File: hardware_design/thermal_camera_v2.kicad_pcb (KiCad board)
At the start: 2 copper layers, 69 x 34 mm, 52 parts, among them J1 Conn_01x04_Female, J2 Conn_01x01_Male, J3 Conn_01x07_Female, J4 Conn_01x01_Female, J5 USB_B_Mini, Q1 AP2312, Q2 AP2311, SW1 DTSMW69N, SW2 DTSMW69N, U1 STM32F205RCTx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

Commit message: Fix button part number, add components BOM
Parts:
- R1, R10, R3, R9: value 4k7 -> 3k3
- SW1, SW2: value DTSMW69N -> 1-1825910-4
- U1: value STM32F205RCTx -> STM32F205RC
- U4: value M25PX32-VMW -> W25Q64
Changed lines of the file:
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@@
       (effects (font (size 1 1) (thickness 0.15)))
     )
-    (fp_text value "4k7" (at 0 1.43 90) (layer "F.Fab")
+    (fp_text value "3k3" (at 0 1.43 90) (layer "F.Fab")
       (effects (font (size 1 1) (thickness 0.15)))
     )
@@
       (effects (font (size 1 1) (thickness 0.15)))
     )
-    (fp_text value "STM32F205RCTx" (at 0 7.4 90) (layer "F.Fab")
+    (fp_text value "STM32F205RC" (at 0 7.4 90) (layer "F.Fab")
       (effects (font (size 1 1) (thickness 0.15)))
     )
@@
       (effects (font (size 1 1) (thickness 0.15)))
     )
-    (fp_text value "4k7" (at 0 1.43 90) (layer "F.Fab")
+    (fp_text value "3k3" (at 0 1.43 90) (layer "F.Fab")
       (effects (font (size 1 1) (thickness 0.15)))
     )
@@
       (effects (font (size 1 1) (thickness 0.15)))
     )
-    (fp_text value "M25PX32-VMW" (at 0 3.68 90) (layer "F.Fab")
+    (fp_text value "W25Q64" (at 0 3.68 90) (layer "F.Fab")
       (effects (font (size 1 1) (thickness 0.15)))
     )
@@
       (effects (font (size 1 1) (thickness 0.15)))
     )
-    (fp_text value "4k7" (at 0 1.43 90) (layer "F.Fab")
+    (fp_text value "3k3" (at 0 1.43 90) (layer "F.Fab")
       (effects (font (size 1 1) (thickness 0.15)))
     )
@@
       (effects (font (size 1 1) (thickness 0.15)))
     )
-    (fp_text value "4k7" (at 0 1.43) (layer "F.Fab")
+    (fp_text value "3k3" (at 0 1.43) (layer "F.Fab")
       (effects (font (size 1 1) (thickness 0.15)))
     )
@@
       (effects (font (size 1 1) (thickness 0.15)) (justify mirror))
     )
-    (fp_text value "DTSMW69N" (at 3.75 -6.7) (layer "B.Fab")
+    (fp_text value "1-1825910-4" (at 3.75 -6.7) (layer "B.Fab")
       (effects (font (size 1 1) (thickness 0.15)) (justify mirror))
     )
@@
       (effects (font (size 1 1) (thickness 0.15)) (justify mirror))
     )
-    (fp_text value "DTSMW69N" (at 3.75 -6.7) (layer "B.Fab")
+    (fp_text value "1-1825910-4" (at 3.75 -6.7) (layer "B.Fab")
       (effects (font (size 1 1) (thickness 0.15)) (justify mirror))
     )

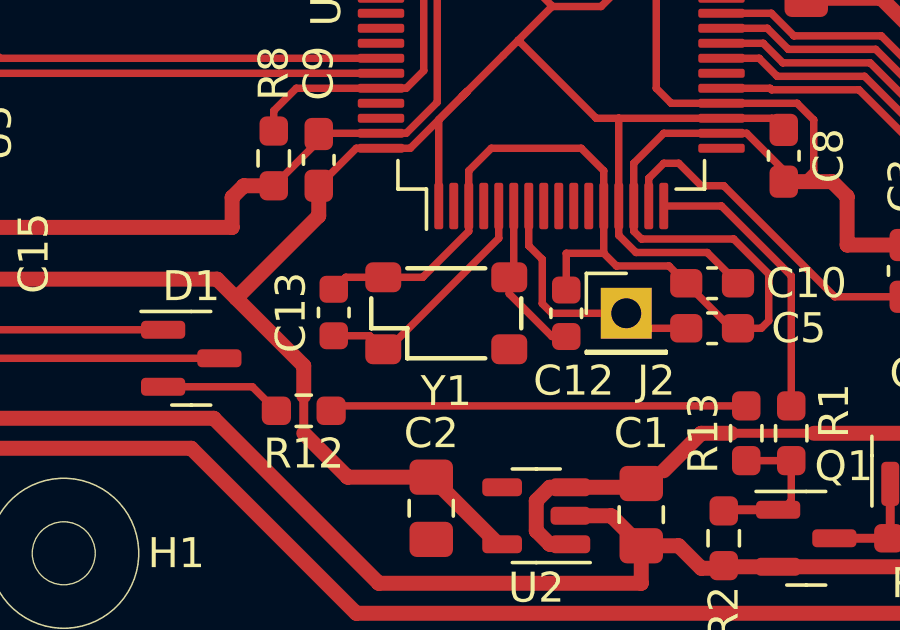
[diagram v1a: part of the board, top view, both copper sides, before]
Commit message: Switched XTAL footprint
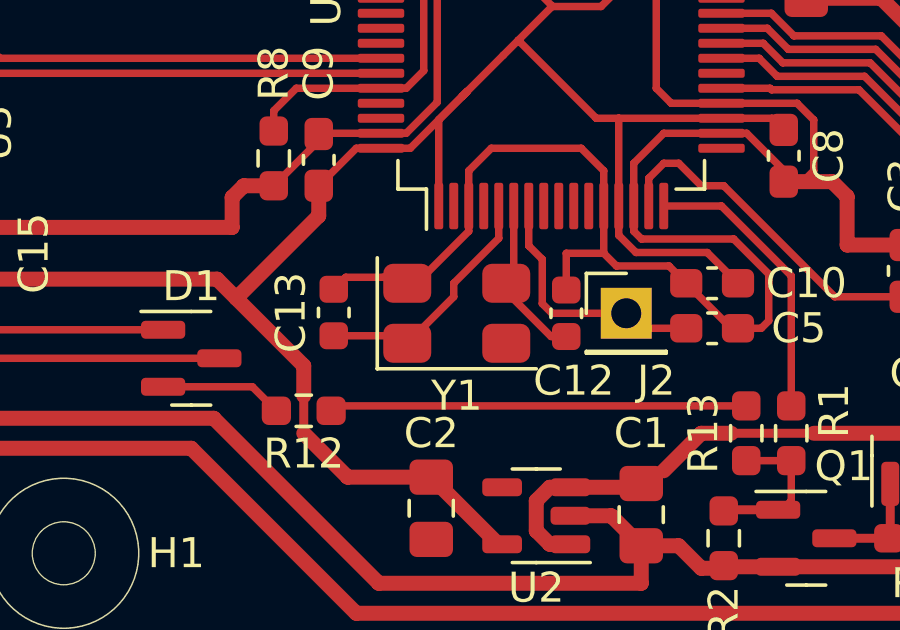
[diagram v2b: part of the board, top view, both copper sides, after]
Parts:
- Y1: footprint TFT_footprints:XTAL_5030_china_unknown -> Crystal:Crystal_SMD_5032-4Pin_5.0x3.2mm
- moved Y1 0.35 mm to (150.8, 110.5)
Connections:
- Y1 pad 3: GND -> Net-(C12-Pad1)
- Y1 pad 4: Net-(C12-Pad1) -> GND
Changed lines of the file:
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@@
     )
-  )
-  (footprint "TFT_footprints:XTAL_5030_china_unknown" (layer "F.Cu")
-    (at 150.5 110.5)
-    (property "Sheetfile" "thermal_camera_v2.kicad_sch")
-    (property "Sheetname" "")
-    (attr through_hole)
-    (fp_text reference "Y1" (at 0 2.6) (layer "F.SilkS")
-      (effects (font (size 1 1) (thickness 0.15)))
-    )
-    (fp_text value "8MHz" (at 0 -2.6) (layer "F.Fab")
-      (effects (font (size 1 1) (thickness 0.15)))
-    )
-    (fp_line (start -2.5 0.5) (end -1.3 0.5) (layer "F.SilkS") (width 0.15))
-    (fp_line (start -2.5 -0.5) (end -2.5 0.5) (layer "F.SilkS") (width 0.15))
-    (fp_line (start -1.3 0.5) (end -1.3 1.5) (layer "F.SilkS") (width 0.15))
-    (fp_line (start 2.5 -0.5) (end 2.5 0.5) (layer "F.SilkS") (width 0.15))
-    (fp_line (start -1.3 -1.5) (end 1.3 -1.5) (layer "F.SilkS") (width 0.15))
-    (fp_line (start -1.3 1.5) (end 1.3 1.5) (layer "F.SilkS") (width 0.15))
-    (pad "1" smd roundrect locked (at -2.1 1.2) (size 1.2 1) (layers "F.Cu" "F.Paste" "F.Mask") (roundrect_rratio 0.25)
-      (net 11 "Net-(C13-Pad1)") (pinfunction "1") (pintype "passive") (zone_connect 0))
-    (pad "2" smd roundrect locked (at 2.1 1.2) (size 1.2 1) (layers "F.Cu" "F.Paste" "F.Mask") (roundrect_rratio 0.25)
-      (net 60 "unconnected-(Y1-Pad2)") (pinfunction "2") (pintype "passive") (zone_connect 0))
-    (pad "3" smd roundrect locked (at -2.1 -1.2) (size 1.2 1) (layers "F.Cu" "F.Paste" "F.Mask") (roundrect_rratio 0.25)
-      (net 2 "GND") (pinfunction "3") (pintype "passive") (zone_connect 0))
-    (pad "4" smd roundrect locked (at 2.1 -1.2) (size 1.2 1) (layers "F.Cu" "F.Paste" "F.Mask") (roundrect_rratio 0.25)
-      (net 10 "Net-(C12-Pad1)") (pinfunction "4") (pintype "passive") (zone_connect 0))
   )
   (footprint "Package_QFP:LQFP-64_10x10mm_P0.5mm" (layer "F.Cu")
@@
       (net 16 "/BOOT0") (pintype "passive"))
     (model "${KICAD6_3DMODEL_DIR}/Resistor_SMD.3dshapes/R_0603_1608Metric.wrl"
+      (offset (xyz 0 0 0))
+      (scale (xyz 1 1 1))
+      (rotate (xyz 0 0 0))
+    )
+  )
+  (footprint "Crystal:Crystal_SMD_5032-4Pin_5.0x3.2mm" (layer "F.Cu")
+    (at 150.85 110.5)
+    (descr "SMD Crystal SERIES SMD2520/4 http://www.icbase.com/File/PDF/HKC/HKC00061008.pdf, 5.0x3.2mm^2 package")
+    (tags "SMD SMT crystal")
+    (property "Sheetfile" "thermal_camera_v2.kicad_sch")
+    (property "Sheetname" "")
+    (attr smd)
+    (fp_text reference "Y1" (at 0 2.75) (layer "F.SilkS")
+      (effects (font (size 1 1) (thickness 0.15)))
+    )
+    (fp_text value "8MHz" (at 0 2.8) (layer "F.Fab")
+      (effects (font (size 1 1) (thickness 0.15)))
+    )
+    (fp_text user "${REFERENCE}" (at 0 0) (layer "F.Fab")
+      (effects (font (size 1 1) (thickness 0.15)))
+    )
+    (fp_line (start -2.65 1.85) (end 2.65 1.85) (layer "F.SilkS") (width 0.12))
+    (fp_line (start -2.65 -1.85) (end -2.65 1.85) (layer "F.SilkS") (width 0.12))
+    (fp_line (start -2.8 -1.9) (end -2.8 1.9) (layer "F.CrtYd") (width 0.05))
+    (fp_line (start 2.8 1.9) (end 2.8 -1.9) (layer "F.CrtYd") (width 0.05))
+    (fp_line (start 2.8 -1.9) (end -2.8 -1.9) (layer "F.CrtYd") (width 0.05))
+    (fp_line (start -2.8 1.9) (end 2.8 1.9) (layer "F.CrtYd") (width 0.05))
+    (fp_line (start -2.3 1.6) (end -2.5 1.4) (layer "F.Fab") (width 0.1))
+    (fp_line (start -2.5 0.6) (end -1.5 1.6) (layer "F.Fab") (width 0.1))
+    (fp_line (start -2.3 -1.6) (end 2.3 -1.6) (layer "F.Fab") (width 0.1))
+    (fp_line (start 2.3 -1.6) (end 2.5 -1.4) (layer "F.Fab") (width 0.1))
+    (fp_line (start 2.3 1.6) (end -2.3 1.6) (layer "F.Fab") (width 0.1))
+    (fp_line (start 2.5 1.4) (end 2.3 1.6) (layer "F.Fab") (width 0.1))
+    (fp_line (start -2.5 -1.4) (end -2.3 -1.6) (layer "F.Fab") (width 0.1))
+    (fp_line (start -2.5 1.4) (end -2.5 -1.4) (layer "F.Fab") (width 0.1))
+    (fp_line (start 2.5 -1.4) (end 2.5 1.4) (layer "F.Fab") (width 0.1))
+    (pad "1" smd roundrect (at -1.65 1) (size 1.6 1.3) (layers "F.Cu" "F.Paste" "F.Mask") (roundrect_rratio 0.25)
+      (net 11 "Net-(C13-Pad1)") (pinfunction "1") (pintype "passive"))
+    (pad "2" smd roundrect (at 1.65 1) (size 1.6 1.3) (layers "F.Cu" "F.Paste" "F.Mask") (roundrect_rratio 0.25)
+      (net 60 "unconnected-(Y1-Pad2)") (pinfunction "2") (pintype "passive"))
+    (pad "3" smd roundrect (at 1.65 -1) (size 1.6 1.3) (layers "F.Cu" "F.Paste" "F.Mask") (roundrect_rratio 0.25)
+      (net 10 "Net-(C12-Pad1)") (pinfunction "3") (pintype "passive"))
+    (pad "4" smd roundrect (at -1.65 -1) (size 1.6 1.3) (layers "F.Cu" "F.Paste" "F.Mask") (roundrect_rratio 0.25)
+      (net 2 "GND") (pinfunction "4") (pintype "passive"))
+    (model "${KICAD6_3DMODEL_DIR}/Crystal.3dshapes/Crystal_SMD_5032-4Pin_5.0x3.2mm.wrl"
       (offset (xyz 0 0 0))
       (scale (xyz 1 1 1))
@@
   (segment (start 147.5 120.5) (end 142 115) (width 0.5) (layer "F.Cu") (net 9))
   (segment (start 168.0125 116.1875) (end 169.95 114.25) (width 0.5) (layer "F.Cu") (net 9))
-  (segment (start 154.025 111.275) (end 152.6 109.85) (width 0.25) (layer "F.Cu") (net 10))
-  (segment (start 152.6 109.85) (end 152.6 109.3) (width 0.25) (layer "F.Cu") (net 10))
-  (segment (start 152.75 106.925) (end 152.75 109.15) (width 0.25) (layer "F.Cu") (net 10))
-  (segment (start 154.5 111.275) (end 154.025 111.275) (width 0.25) (layer "F.Cu") (net 10))
-  (segment (start 152.75 109.15) (end 152.6 109.3) (width 0.25) (layer "F.Cu") (net 10))
+  (segment (start 153.993559 111.275) (end 152.5 109.781441) (width 0.25) (layer "F.Cu") (net 10))
+  (segment (start 152.5 109.781441) (end 152.5 109.5) (width 0.25) (layer "F.Cu") (net 10))
+  (segment (start 152.75 106.925) (end 152.75 109.25) (width 0.25) (layer "F.Cu") (net 10))
+  (segment (start 154.5 111.275) (end 153.993559 111.275) (width 0.25) (layer "F.Cu") (net 10))
+  (segment (start 152.75 109.25) (end 152.5 109.5) (width 0.25) (layer "F.Cu") (net 10))
+  (segment (start 146.75 111.25) (end 148.95 111.25) (width 0.25) (layer "F.Cu") (net 11))
+  (segment (start 152.25 108) (end 150.75 109.5) (width 0.25) (layer "F.Cu") (net 11))
   (segment (start 152.25 106.925) (end 152.25 108) (width 0.25) (layer "F.Cu") (net 11))
-  (segment (start 148.55 111.7) (end 148.4 111.7) (width 0.25) (layer "F.Cu") (net 11))
-  (segment (start 152.25 108) (end 148.55 111.7) (width 0.25) (layer "F.Cu") (net 11))
-  (segment (start 147.95 111.25) (end 148.4 111.7) (width 0.25) (layer "F.Cu") (net 11))
-  (segment (start 146.75 111.25) (end 147.95 111.25) (width 0.25) (layer "F.Cu") (net 11))
+  (segment (start 150.75 109.5) (end 150.75 109.95) (width 0.25) (layer "F.Cu") (net 11))
+  (segment (start 148.95 111.25) (end 149.2 111.5) (width 0.25) (layer "F.Cu") (net 11))
+  (segment (start 150.75 109.95) (end 149.2 111.5) (width 0.25) (layer "F.Cu") (net 11))
   (segment (start 128.535978 99.214022) (end 128.535978 107.785978) (width 0.25) (layer "F.Cu") (net 12))
   (segment (start 131.8 111.05) (end 141.0625 111.05) (width 0.25) (layer "F.Cu") (net 12))
